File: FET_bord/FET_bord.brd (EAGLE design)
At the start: 85 x 54 mm, 70 parts

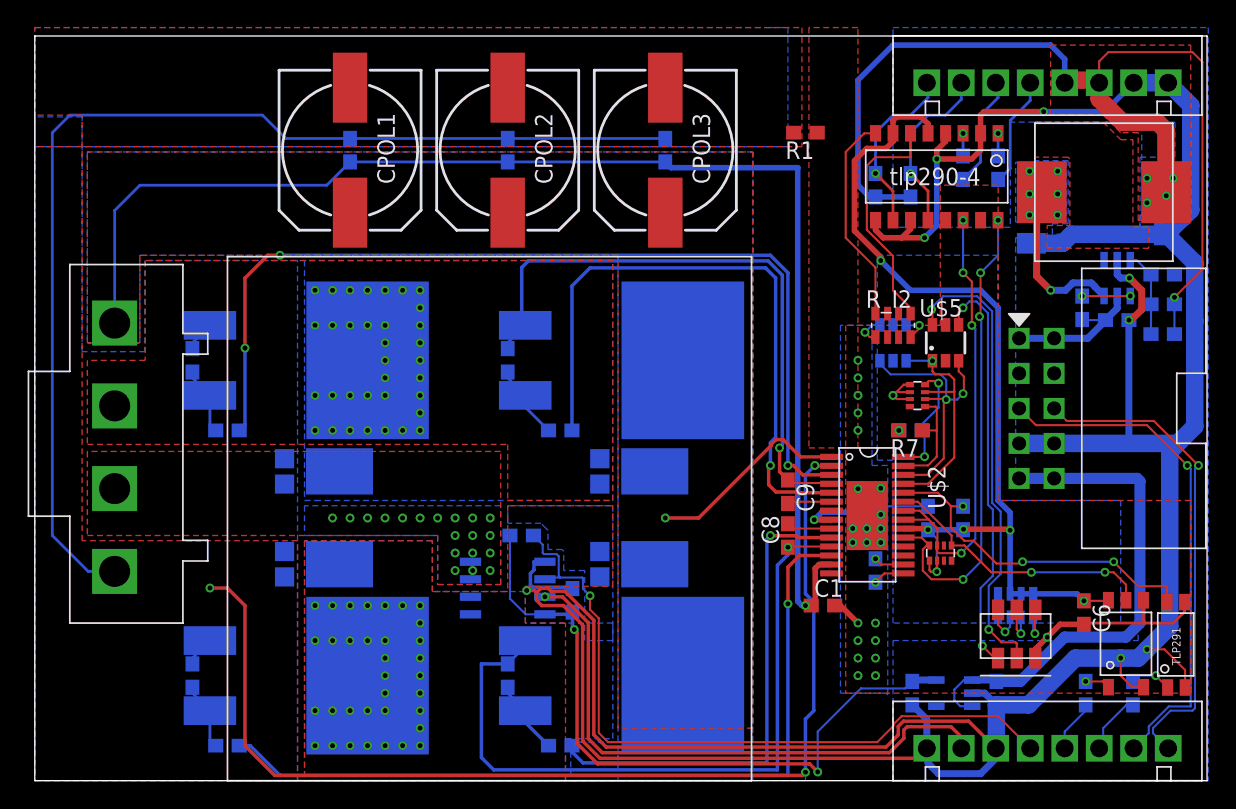
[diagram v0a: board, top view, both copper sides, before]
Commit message: 設計終了、DRC通った。がばでたを出力した
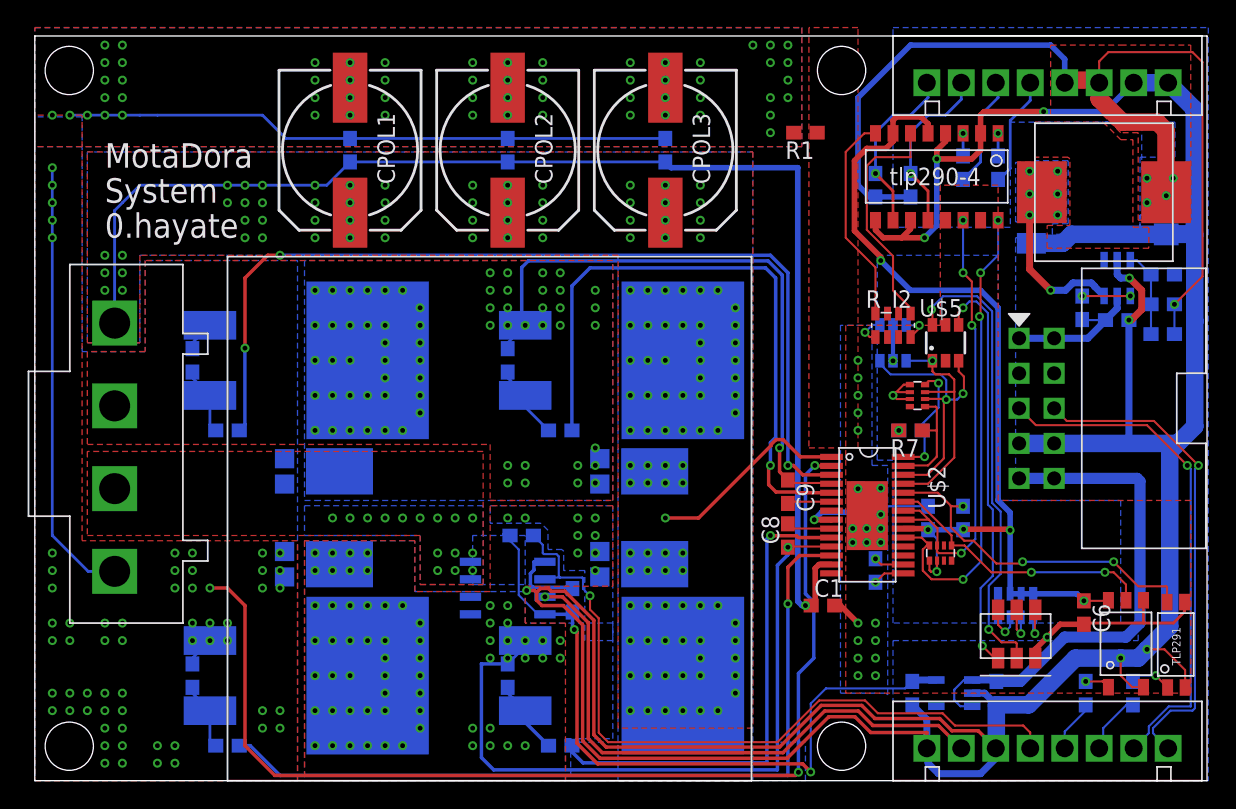
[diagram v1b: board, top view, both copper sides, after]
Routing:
- net GND: track 164.0 -> 159.4 mm, vias 3 -> 120
- net GNDINT: track 250.6 -> 255.2 mm
- net GNDI: track 25.0 -> 27.6 mm, vias 24 -> 25
- net SENS_VCC: track 50.7 -> 52.3 mm
- net FAULT: track 52.3 -> 53.8 mm
- net N$2: track 13.0 -> 11.5 mm
- net 12V: track 11.2 -> 10.6 mm
- net VDD: vias 2 -> 133
- net SB: vias 35 -> 65
- net SA: vias 35 -> 73
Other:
- board text added: "0.hayate"
- board text added: "MotaDora"
- board text added: "System"

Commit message: mcu側に着手
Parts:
- removed R19: (no value), user_rcl:1608
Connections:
- removed net FAULT: CON2.P$4, R19.1, U$3.P$6
- net +3V3: no longer CON1.P$5
- net 5V: now also CON1.P$5
- net SENS_VCC: now also CON2.P$4; no longer R19.2
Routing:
- net FAULT: track 53.8 -> 0.00 mm, vias 1 -> 0
- net 5V: track 36.9 -> 86.8 mm
- net SENS_VCC: track 52.3 -> 59.8 mm, vias 2 -> 3
- net +3V3: track 73.7 -> 72.7 mm
